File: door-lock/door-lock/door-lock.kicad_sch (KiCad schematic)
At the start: 13 parts, among them J1 Barrel_Jack, K1 Relay_SPDT, Q1 2N3904, Q2 2N3904, U2 LM7805_TO220

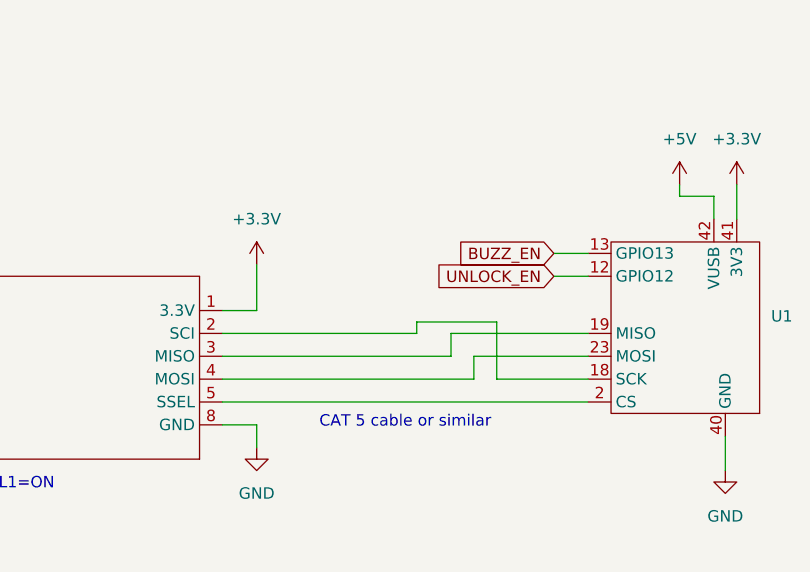
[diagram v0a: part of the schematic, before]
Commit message: timeout wifi connection if unavailable
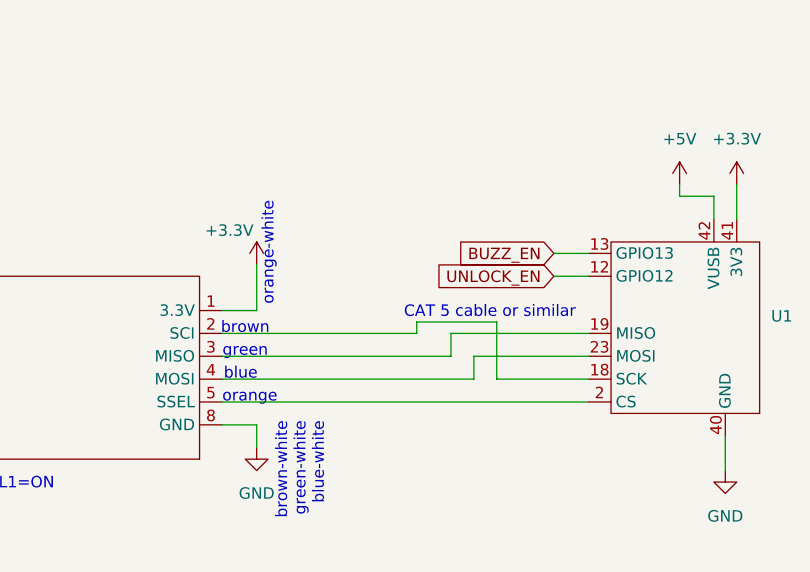
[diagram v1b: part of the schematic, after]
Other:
- note added: "blue"
- note added: "brown"
- note added: "brown-white green-white blue-white"
- note added: "green"
- note added: "orange"
- note added: "orange-white"
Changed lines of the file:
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@@
 	(generator_version "9.0")
 	(paper "A4")
+	(text "brown-white\ngreen-white\nblue-white"
+		(exclude_from_sim no)
+		(at 87.376 119.126 90)
+		(effects
+			(font
+				(size 1.27 1.27)
+			)
+			(justify right)
+		)
+	)
+	(text "orange"
+		(exclude_from_sim no)
+		(at 81.788 116.332 0)
+		(effects
+			(font
+				(size 1.27 1.27)
+			)
+		)
+	)
+	(text "orange-white"
+		(exclude_from_sim no)
+		(at 83.82 106.172 90)
+		(effects
+			(font
+				(size 1.27 1.27)
+			)
+			(justify left)
+		)
+	)
+	(text "blue"
+		(exclude_from_sim no)
+		(at 80.772 113.792 0)
+		(effects
+			(font
+				(size 1.27 1.27)
+			)
+		)
+	)
+	(text "brown"
+		(exclude_from_sim no)
+		(at 81.28 108.712 0)
+		(effects
+			(font
+				(size 1.27 1.27)
+			)
+		)
+	)
 	(text "COAX or similar cable"
 		(exclude_from_sim no)
@@
 	(text "CAT 5 cable or similar"
 		(exclude_from_sim no)
-		(at 99.06 119.126 0)
+		(at 108.458 106.934 0)
+		(effects
+			(font
+				(size 1.27 1.27)
+			)
+		)
+	)
+	(text "green"
+		(exclude_from_sim no)
+		(at 81.28 111.252 0)
 		(effects
 			(font
@@
 		(on_board yes)
 		(dnp no)
-		(fields_autoplaced yes)
 		(property "Reference" "#PWR09"
 			(at 82.55 105.41 0)
@@
 		)
 		(property "Value" "+3.3V"
-			(at 82.55 96.52 0)
-			(effects
-				(font
+			(at 79.502 97.79 0)
+			(effects
+				(font
